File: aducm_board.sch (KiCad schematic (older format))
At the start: 66 parts, among them J1 USB_B_Micro, J3 Conn_02x04_Odd_Even, J6 JST_PH, SW1 SW_Push, U1 aducm_355, U2 FT232RL, U3 SPX3819M5-L-3-3, U4 MCP73831-2-OT, Y1 32MHz

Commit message: added initial board layout
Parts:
- removed C1, C12, C2: 0.1uF, Capacitor_SMD:C_0603_1608Metric, symbol Device:C
- removed D1, D2: D_Schottky, symbol Device:D_Schottky
- removed JP1, JP2: Jumper_NC_Small, symbol Device:Jumper_NC_Small
- removed R6, R7, R8: 0, Resistor_SMD:R_0603_1608Metric, symbol Device:R_Small_US
- removed U2: FT232RL, Button_Switch_SMD:SW_SPST_B3S-1000, symbol Interface_USB:FT232RL
- removed U3: SPX3819M5-L-3-3, Package_TO_SOT_SMD:SOT-23-5, symbol Regulator_Linear:SPX3819M5-L-3-3
- C13, C4: value 7pF -> 6pF
- D3: footprint (none) -> LED_SMD:LED_0805_2012Metric
- J6: footprint (none) -> Connector_JST:JST_PH_S2B-PH-SM4-TB_1x02-1MP_P2.00mm_Horizontal
- Y1: footprint (none) -> Crystal:Crystal_SMD_Abracon_ABM10-4Pin_2.5x2.0mm
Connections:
- net labels removed: 3V3VOUT, P0.10_SOUT, P0.11_SIN, SDIO
- wire segments 245 -> 209
- no-connect marks 12 -> 1
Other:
- note removed: "FTDI USB to UART"

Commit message: Removed unnecessary components
Move things like the Battery Charging circuitry to a separate sheet that can be readded in the future.
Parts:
- removed C14, C15, C21: 10uF, Capacitor_SMD:C_0603_1608Metric, symbol Device:C
- removed C19, C20, C3, C43, C44, C5, C6: 0.1uF, Capacitor_SMD:C_0603_1608Metric, symbol Device:C
- removed D3: LED, LED_SMD:LED_0805_2012Metric, symbol Device:LED
- removed FB1, FB2: Ferrite_Bead_Small, Inductor_SMD:L_0603_1608Metric, symbol Device:Ferrite_Bead_Small
- removed FB3, FB4: 60Ohm at 100Mhz, Inductor_SMD:L_0603_1608Metric, symbol Device:Ferrite_Bead_Small
- removed J1: USB_B_Micro, Connector_USB:USB_Micro-B_Amphenol_10103594-0001LF_Horizontal, symbol Connector:USB_B_Micro
- removed J6: JST_PH, Connector_JST:JST_PH_S2B-PH-SM4-TB_1x02-1MP_P2.00mm_Horizontal, symbol Connector_Generic:Conn_01x02
- removed R15: 2k, Resistor_SMD:R_0603_1608Metric, symbol Device:R_Small_US
- removed R16: 440, Resistor_SMD:R_0603_1608Metric, symbol Device:R_Small_US
- removed R3, R4: 2.2, Resistor_SMD:R_0603_1608Metric, symbol Device:R_Small_US
- removed U4: MCP73831-2-OT, Package_TO_SOT_SMD:SOT-23-5, symbol Battery_Management:MCP73831-2-OT
- renumbered C4 to C1, C18 to C10, C22 to C11, C23 to C12, C24 to C13, C25 to C14, C26 to C15, C27 to C16, C28 to C17, C29 to C18, C30 to C19, C7 to C2, C31 to C20, C32 to C21, C33 to C22, C34 to C23, C35 to C24, C36 to C25, C8 to C3, C9 to C4, C10 to C5, C11 to C6, C13 to C7, C16 to C8, C17 to C9, J3 to J1, R5 to R3
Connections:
- net AVDD is gone; now on net GNDA: C10.1, U1.F11 (AVDD)
- net GNDD is gone; now on net GNDA: C1.2, C16.2, C23.2, C25.2, C7.2, C8.2, C9.2, J1.2 (Pin_2), SW1.2, U1.F2 (DGND_AD), U1.F7 (DGND), U1.H2 (AGND_DD), Y1.2, Y1.4
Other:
- note removed: "External Power Filtering"
- note removed: "FBTH1608HE600-T"
- note removed: "LiPo Battery Charging from USB"
- note removed: "LiPo Battery Input"
- note removed: "USB Input"

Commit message: first version of pcb aducm355 on board
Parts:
- U1: footprint ADUCM355:aducm355 -> aducm_board:aducm355
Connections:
- net AIN3: now also U1.B7 (AIN3/BUF_VREF1V8)
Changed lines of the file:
@@
 EESchema Schematic File Version 4
+LIBS:aducm_board-cache
 EELAYER 30 0
 EELAYER END
@@
 F 0 "U1" H 10050 6315 50  0000 C CNN
 F 1 "aducm_355" H 10050 6224 50  0000 C CNN
-F 2 "ADUCM355:aducm355" H 10050 4350 50  0001 C CNN
+F 2 "aducm_board:aducm355" H 10050 4350 50  0001 C CNN
 F 3 "" H 10050 4350 50  0001 C CNN
 	1    10000 4400
@@
 	2250 800  2250 850
 Connection ~ 2250 850
+Text Label 8400 5300 0    50   ~ 0
+AIN3
+Wire Wire Line
+	8400 5300 8850 5300
 $EndSCHEMATC

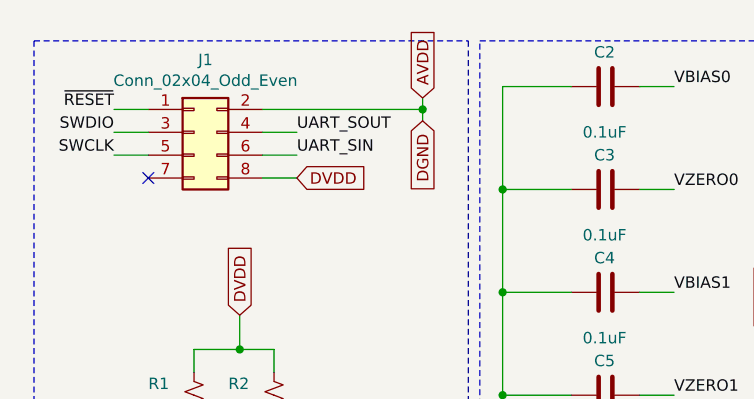
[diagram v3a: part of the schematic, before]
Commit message: Started Fixing AGND AVDD Flip Flop
The Schematic is not complete to reflect the changes yet
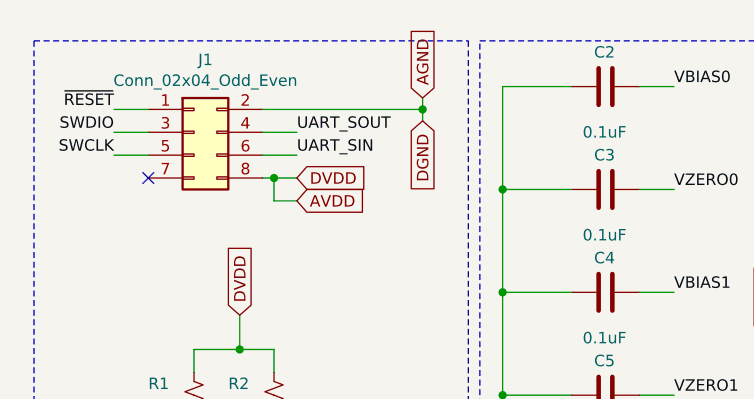
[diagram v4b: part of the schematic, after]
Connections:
- net GNDA: no longer C10.1, U1.F11 (AVDD)
- net DVDD renamed AVDD
- net AVDD: now also C10.1, U1.F11 (AVDD)
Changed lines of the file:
@@
 EESchema Schematic File Version 4
-LIBS:aducm_board-cache
 EELAYER 30 0
 EELAYER END
@@
 	1700 1050 1550 1050
 Wire Wire Line
-	1550 1150 1700 1150
+	1550 1150 1600 1150
 Wire Wire Line
 	1050 1050 900  1050
@@
 Text GLabel 1300 3200 0    50   Input ~ 0
 AGND
-Text GLabel 2250 800  1    50   Input ~ 0
-AVDD
 Wire Wire Line
 	2250 800  2250 850
@@
 Wire Wire Line
 	8400 5300 8850 5300
+Text GLabel 2250 800  1    50   Input ~ 0
+AGND
+Text GLabel 1700 1250 2    50   Input ~ 0
+AVDD
+Wire Wire Line
+	1700 1250 1600 1250
+Wire Wire Line
+	1600 1250 1600 1150
+Connection ~ 1600 1150
+Wire Wire Line
+	1600 1150 1700 1150
 $EndSCHEMATC

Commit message: cleaning
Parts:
- U1: footprint aducm_board:aducm355 -> SIB_Generic:aducm355; symbol chemcrab:aducm_355 -> SIB_Footprint:aducm_355
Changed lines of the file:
@@
 EESchema Schematic File Version 4
+LIBS:aducm_board-cache
 EELAYER 30 0
 EELAYER END
@@
 $EndDescr
 $Comp
-L chemcrab:aducm_355 U1
+L SIB_Footprint:aducm_355 U1
 U 1 1 5DDA438D
 P 10000 4400
 F 0 "U1" H 10050 6315 50  0000 C CNN
 F 1 "aducm_355" H 10050 6224 50  0000 C CNN
-F 2 "aducm_board:aducm355" H 10050 4350 50  0001 C CNN
+F 2 "SIB_Generic:aducm355" H 10050 4350 50  0001 C CNN
 F 3 "" H 10050 4350 50  0001 C CNN
 	1    10000 4400
